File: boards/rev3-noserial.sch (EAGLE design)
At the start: 37 parts, among them J1 10103594-0001LF, U1 ESP-WROOM-32, U3 SP0503BAHT, U4 CP2102N-A01-GQFN28

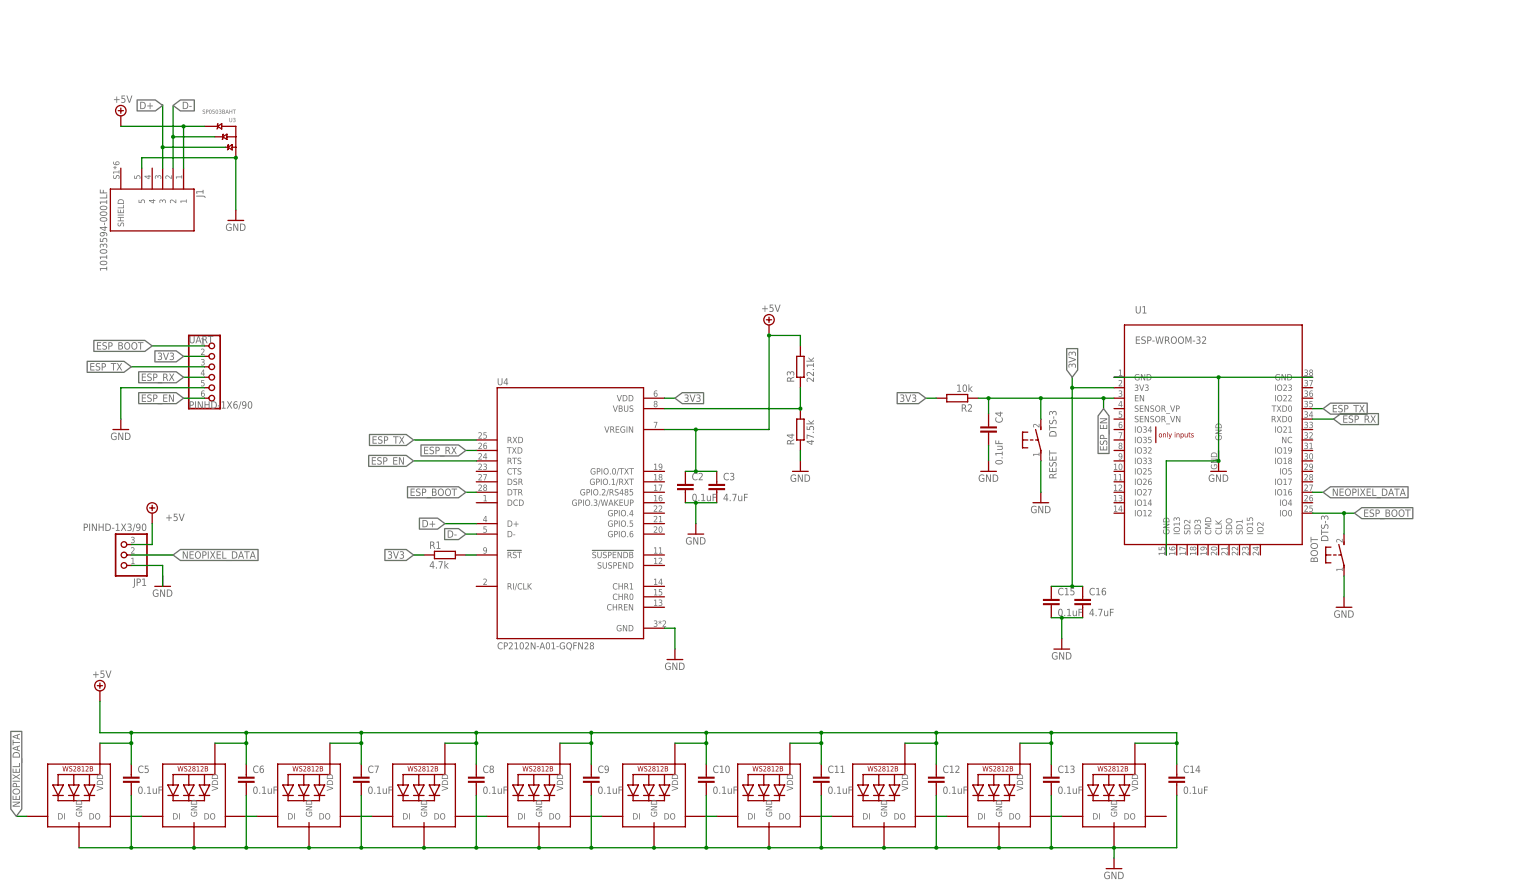
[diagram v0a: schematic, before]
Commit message: Introduce rev3 and remove non-functional d-board.
The d-shaped board never worked, remove it.

The new rev3 is not meant to replace the existing boards in the AliExpress bases but rather includes its own 3D-printed base.
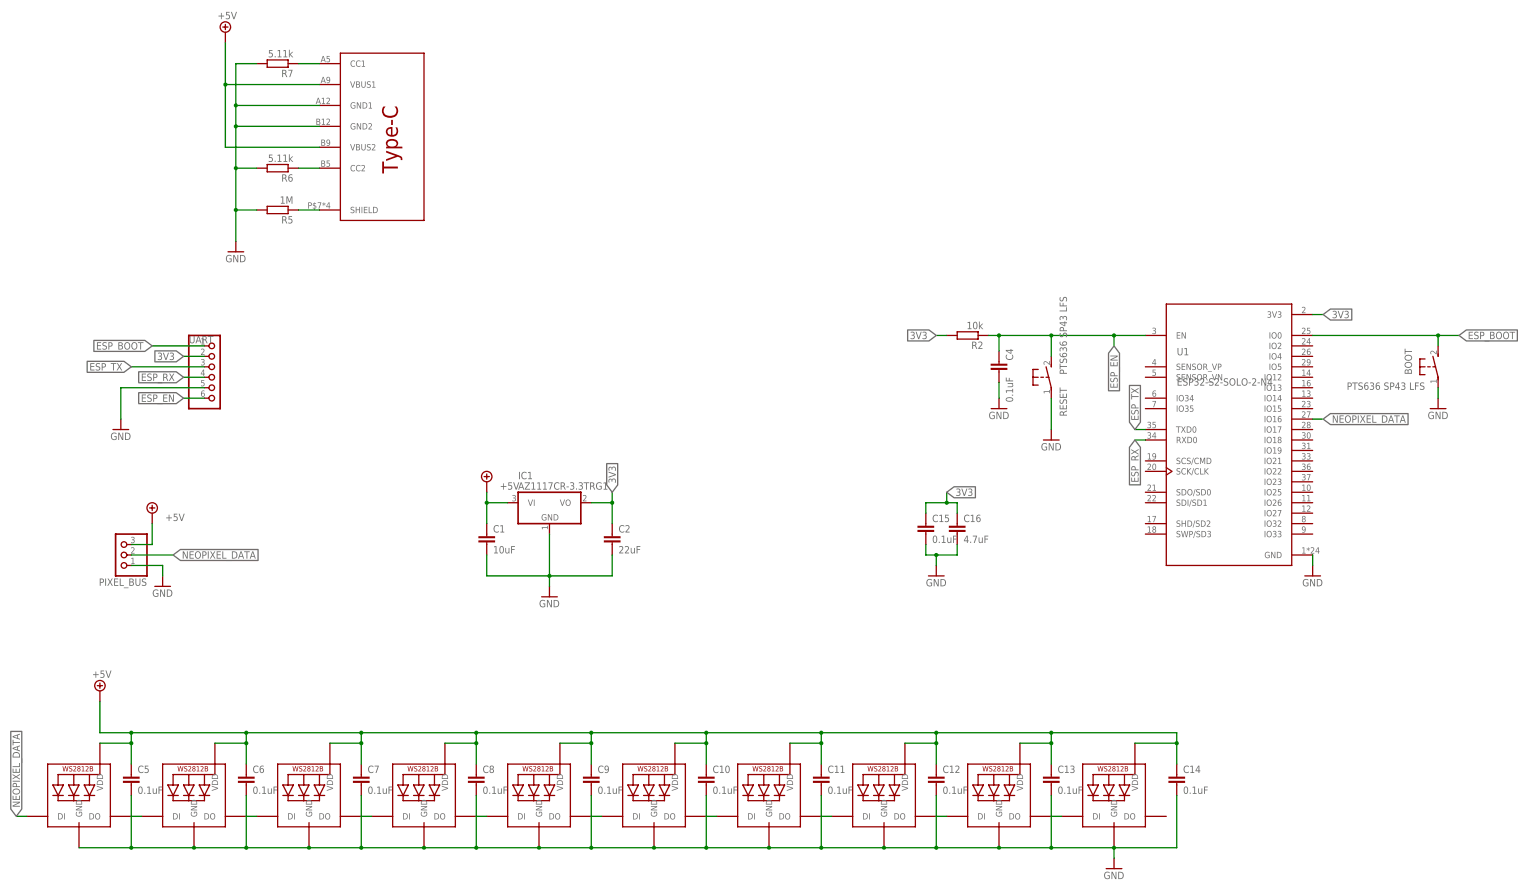
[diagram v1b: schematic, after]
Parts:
- removed C3: 4.7uF, rcl:C-EUC0805
- removed J1: 10103594-0001LF, 10103594-0001LF:10103594-0001LF
- removed JP1: PINHD-1X3/90, Connector:PINHD-1X3/90
- removed R1: 4.7k, rcl:R-EU_R0805
- removed R3: 22.1k, rcl:R-EU_R0805
- removed R4: 47.5k, rcl:R-EU_R0805
- removed U3: SP0503BAHT, SP0503BAHT:SP0503BAHT
- removed U4: CP2102N-A01-GQFN28, CP2102N-A01-GQFN28:CP2102N-A01-GQFN28
- added C1: 10uF, rcl:C-EUC0805
- added IC1: AZ1117CR-3.3TRG1, flameeyes:AZ1117CR
- added PIXEL_BUS: (no value), pinhead:PINHD-1X3
- added R5: 1M, rcl:R-EU_R0805
- added R6, R7: 5.11k, rcl:R-EU_R0805
- added U$1: TYPEC-DB-104PWB, flameeyes:TYPEC-DB-104PWB
- BOOT, RESET: value DTS-3 -> PTS636 SP43 LFS; device switch-tact:DTS-3 -> flameeyes:PTS636SP43LFS
- C2: value 0.1uF -> 22uF
- LED1, LED10, LED2, LED3, LED4, LED5, LED6, LED7, LED8, LED9: device adafruit:WS2812B5050 -> flameeyes:WS2812B5050
- U1: value ESP-WROOM-32 -> ESP32-S2-SOLO-2-N4; device esp32:ESP-WROOM-32 -> ESP32-WROOM-32D:ESP32-WROOM-32D
- UART: value PINHD-1X6/90 -> (none); device Connector:PINHD-1X6/90 -> pinhead:PINHD-1X6
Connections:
- removed net D+: J1.3, U3.A, U4.D+
- removed net D-: J1.2, U3.B, U4.D-
- removed net N$5: R1.2, U4.!RST
- new net N$1: R6.1, U$1.CC2
- new net N$2: R5.1, U$1.SHIELD
- net +5V: now also C1.1, IC1.VI, PIXEL_BUS.3, U$1.VBUS1, U$1.VBUS2; no longer C2.1, C3.1, J1.1, JP1.3, R3.2, U3.C, U4.VREGIN
- net 3V3: now also C2.1, IC1.VO; no longer R1.1, U4.VDD
- net ESP_BOOT: no longer U4.DTR
- net ESP_EN: no longer U4.RTS
- net ESP_RX: no longer U4.TXD
- net ESP_TX: no longer U4.RXD
- net GND: now also C1.2, IC1.GND, PIXEL_BUS.1, R5.2, R6.2, R7.2, U$1.GND1, U$1.GND2; no longer C3.2, J1.5, JP1.1, R4.1, U1.GND@1, U1.GND@15, U1.GND@38, U3.GND, U4.GND
- net N$3: now also R7.1, U$1.CC1; no longer R3.1, R4.2, U4.VBUS
- net NEOPIXEL_DATA: now also PIXEL_BUS.2; no longer JP1.2
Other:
- moved on the sheet: BOOT, C15, C16, C2, C4, R2, RESET

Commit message: Update the no-serial design for autoprogram.
This includes the same design block as the ESP32 WROOM-like modules, which means it should be possible to auto-program the boards without needing to solder in buttons.
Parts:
- added Q1, Q2: L8050QLT1G, Transistor:NPN_BC846A,215_SOT23-BEC
- added R1, R3: 10K, rcl:R-EU_R0805
- added R4, R8: 0, rcl:R-EU_R0805
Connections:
- new net !DTR: Q2.E, R1.1, UART.1
- new net !RTS: Q1.E, R3.1, UART.6
- new net N$10: Q1.C, R4.1
- new net N$11: Q2.C, R8.1
- new net N$5: Q1.B, R1.2
- new net N$6: Q2.B, R3.2
- net ESP_BOOT: now also R8.2; no longer UART.1
- net ESP_EN: now also R4.2; no longer UART.6
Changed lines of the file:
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@@
 <schematic_group name="ESP32"/>
 <schematic_group name="VREG"/>
+<schematic_group name="AUTO_PROGRAM1"/>
 </groups>
 <parts>
@@
 <part name="C2" library="rcl" library_urn="urn:adsk.eagle:library:334" deviceset="C-EU" device="C0805" package3d_urn="urn:adsk.eagle:package:23617/2" value="22uF"/>
 <part name="U$1" library="flameeyes" library_urn="urn:adsk.eagle:library:40561536" deviceset="TYPEC-DB-104PWB" device="" package3d_urn="urn:adsk.eagle:package:40563571/2" value="TYPEC-DB-104PWB"/>
+<part name="Q1" library="Transistor" deviceset="NPN_" device="_SOT23-BEC" package3d_urn="urn:adsk.eagle:package:16378725/1" technology="BC846A,215" value="L8050QLT1G"/>
+<part name="Q2" library="Transistor" deviceset="NPN_" device="_SOT23-BEC" package3d_urn="urn:adsk.eagle:package:16378725/1" technology="BC846A,215" value="L8050QLT1G"/>
+<part name="R1" library="rcl" library_urn="urn:adsk.eagle:library:334" deviceset="R-EU_" device="R0805" package3d_urn="urn:adsk.eagle:package:23553/2" value="10K"/>
+<part name="R3" library="rcl" library_urn="urn:adsk.eagle:library:334" deviceset="R-EU_" device="R0805" package3d_urn="urn:adsk.eagle:package:23553/2" value="10K"/>
+<part name="R4" library="rcl" library_urn="urn:adsk.eagle:library:334" deviceset="R-EU_" device="R0805" package3d_urn="urn:adsk.eagle:package:23553/2" value="0"/>
+<part name="R8" library="rcl" library_urn="urn:adsk.eagle:library:334" deviceset="R-EU_" device="R0805" package3d_urn="urn:adsk.eagle:package:23553/2" value="0"/>
 </parts>
 <sheets>
@@
 </instance>
 <instance part="U$1" gate="G$1" x="27.94" y="53.34" smashed="yes" grouprefs="USB_PORT"/>
+<instance part="Q1" gate="G$1" x="106.68" y="55.88" smashed="yes" grouprefs="AUTO_PROGRAM1">
+<attribute name="NAME" x="107.22" y="58.88" size="1.778" layer="95"/>
+<attribute name="VALUE" x="107.22" y="56.34" size="1.778" layer="96"/>
+</instance>
+<instance part="Q2" gate="G$1" x="106.68" y="38.1" smashed="yes" rot="MR180" grouprefs="AUTO_PROGRAM1">
+<attribute name="NAME" x="107.22" y="35.1" size="1.778" layer="95" rot="MR180"/>
+<attribute name="VALUE" x="107.22" y="37.64" size="1.778" layer="96" rot="MR180"/>
+</instance>
+<instance part="R1" gate="G$1" x="93.98" y="55.88" smashed="yes" grouprefs="AUTO_PROGRAM1">
+<attribute name="NAME" x="90.17" y="57.3786" size="1.778" layer="95"/>
+<attribute name="VALUE" x="90.17" y="52.578" size="1.778" layer="96"/>
+</instance>
+<instance part="R3" gate="G$1" x="93.98" y="38.1" smashed="yes" grouprefs="AUTO_PROGRAM1">
+<attribute name="NAME" x="90.17" y="39.5986" size="1.778" layer="95"/>
+<attribute name="VALUE" x="90.17" y="34.798" size="1.778" layer="96"/>
+</instance>
+<instance part="R4" gate="G$1" x="127" y="66.04" smashed="yes" grouprefs="AUTO_PROGRAM1">
+<attribute name="NAME" x="123.19" y="67.5386" size="1.778" layer="95"/>
+<attribute name="VALUE" x="123.19" y="62.738" size="1.778" layer="96"/>
+</instance>
+<instance part="R8" gate="G$1" x="127" y="27.94" smashed="yes" grouprefs="AUTO_PROGRAM1">
+<attribute name="NAME" x="123.19" y="29.4386" size="1.778" layer="95"/>
+<attribute name="VALUE" x="123.19" y="24.638" size="1.778" layer="96"/>
+</instance>
 </instances>
 <busses>
@@
 </segment>
 <segment>
-<pinref part="UART" gate="A" pin="1"/>
-<wire x1="-10.16" y1="-2.54" x2="-22.86" y2="-2.54" width="0.1524" layer="91" grouprefs="UART_HDR"/>
-<label x="-22.86" y="-2.54" size="1.778" layer="95" rot="R180" xref="yes" grouprefs="UART_HDR"/>
+<wire x1="132.08" y1="27.94" x2="137.16" y2="27.94" width="0.1524" layer="91" grouprefs="AUTO_PROGRAM1"/>
+<label x="137.16" y="27.94" size="1.778" layer="95" xref="yes" grouprefs="AUTO_PROGRAM1"/>
+<pinref part="R8" gate="G$1" pin="2"/>
 </segment>
 </net>
@@
 </segment>
 <segment>
-<pinref part="UART" gate="A" pin="6"/>
-<wire x1="-10.16" y1="-15.24" x2="-15.24" y2="-15.24" width="0.1524" layer="91" grouprefs="UART_HDR"/>
-<label x="-15.24" y="-15.24" size="1.778" layer="95" rot="R180" xref="yes" grouprefs="UART_HDR"/>
+<wire x1="132.08" y1="66.04" x2="137.16" y2="66.04" width="0.1524" layer="91" grouprefs="AUTO_PROGRAM1"/>
+<label x="137.16" y="66.04" size="1.778" layer="95" xref="yes" grouprefs="AUTO_PROGRAM1"/>
+<pinref part="R4" gate="G$1" pin="2"/>
 </segment>
 </net>
@@
 </segment>
 </net>
+<net name="N$5" class="0">
+<segment>
+<wire x1="99.06" y1="55.88" x2="101.6" y2="55.88" width="0.1524" layer="91" grouprefs="AUTO_PROGRAM1"/>
+<pinref part="Q1" gate="G$1" pin="B"/>
+<pinref part="R1" gate="G$1" pin="2"/>
+</segment>
+</net>
+<net name="N$6" class="0">
+<segment>
+<wire x1="99.06" y1="38.1" x2="101.6" y2="38.1" width="0.1524" layer="91" grouprefs="AUTO_PROGRAM1"/>
+<pinref part="Q2" gate="G$1" pin="B"/>
+<pinref part="R3" gate="G$1" pin="2"/>
+</segment>
+</net>
+<net name="!DTR" class="0">
+<segment>
+<wire x1="88.9" y1="55.88" x2="86.36" y2="55.88" width="0.1524" layer="91" grouprefs="AUTO_PROGRAM1"/>
+<pinref part="Q2" gate="G$1" pin="E"/>
+<wire x1="86.36" y1="55.88" x2="76.2" y2="55.88" width="0.1524" layer="91" grouprefs="AUTO_PROGRAM1"/>
+<wire x1="106.68" y1="43.18" x2="106.68" y2="45.72" width="0.1524" layer="91" grouprefs="AUTO_PROGRAM1"/>
+<wire x1="106.68" y1="45.72" x2="86.36" y2="45.72" width="0.1524" layer="91" grouprefs="AUTO_PROGRAM1"/>
+<wire x1="86.36" y1="45.72" x2="86.36" y2="55.88" width="0.1524" layer="91" grouprefs="AUTO_PROGRAM1"/>
+<junction x="86.36" y="55.88" grouprefs="AUTO_PROGRAM1"/>
+<label x="76.2" y="55.88" size="1.778" layer="95" rot="R180" xref="yes" grouprefs="AUTO_PROGRAM1"/>
+<pinref part="R1" gate="G$1" pin="1"/>
+</segment>
+<segment>
+<pinref part="UART" gate="A" pin="1"/>
+<wire x1="-10.16" y1="-2.54" x2="-15.24" y2="-2.54" width="0.1524" layer="91"/>
+<label x="-15.24" y="-2.54" size="1.778" layer="95" rot="R90" xref="yes"/>
+</segment>
+</net>
+<net name="N$10" class="0">
+<segment>
+<pinref part="Q1" gate="G$1" pin="C"/>
+<wire x1="106.68" y1="60.96" x2="106.68" y2="66.04" width="0.1524" layer="91" grouprefs="AUTO_PROGRAM1"/>
+<wire x1="106.68" y1="66.04" x2="121.92" y2="66.04" width="0.1524" layer="91" grouprefs="AUTO_PROGRAM1"/>
+<pinref part="R4" gate="G$1" pin="1"/>
+</segment>
+</net>
+<net name="N$11" class="0">
+<segment>
+<pinref part="Q2" gate="G$1" pin="C"/>
+<wire x1="106.68" y1="33.02" x2="106.68" y2="27.94" width="0.1524" layer="91" grouprefs="AUTO_PROGRAM1"/>
+<wire x1="106.68" y1="27.94" x2="121.92" y2="27.94" width="0.1524" layer="91" grouprefs="AUTO_PROGRAM1"/>
+<pinref part="R8" gate="G$1" pin="1"/>
+</segment>
+</net>
+<net name="!RTS" class="0">
+<segment>
+<wire x1="88.9" y1="38.1" x2="83.82" y2="38.1" width="0.1524" layer="91" grouprefs="AUTO_PROGRAM1"/>
+<wire x1="83.82" y1="38.1" x2="76.2" y2="38.1" width="0.1524" layer="91" grouprefs="AUTO_PROGRAM1"/>
+<junction x="83.82" y="38.1" grouprefs="AUTO_PROGRAM1"/>
+<wire x1="83.82" y1="38.1" x2="83.82" y2="48.26" width="0.1524" layer="91" grouprefs="AUTO_PROGRAM1"/>
+<wire x1="83.82" y1="48.26" x2="106.68" y2="48.26" width="0.1524" layer="91" grouprefs="AUTO_PROGRAM1"/>
+<wire x1="106.68" y1="48.26" x2="106.68" y2="50.8" width="0.1524" layer="91" grouprefs="AUTO_PROGRAM1"/>
+<pinref part="Q1" gate="G$1" pin="E"/>
+<label x="76.2" y="38.1" size="1.778" layer="95" rot="R180" xref="yes" grouprefs="AUTO_PROGRAM1"/>
+<pinref part="R3" gate="G$1" pin="1"/>
+</segment>
+<segment>
+<pinref part="UART" gate="A" pin="6"/>
+<wire x1="-10.16" y1="-15.24" x2="-15.24" y2="-15.24" width="0.1524" layer="91"/>
+<label x="-15.24" y="-15.24" size="1.778" layer="95" rot="R180" xref="yes"/>
+</segment>
+</net>
